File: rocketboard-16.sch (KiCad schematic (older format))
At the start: 108 parts, among them J1 SWD, K1 MX_RGB, K10 MX_RGB, K11 MX_RGB, K12 MX_RGB, K13 MX_RGB, K14 MX_RGB, K15 MX_RGB, K16 MX_RGB, K2 MX_RGB, K3 MX_RGB, K4 MX_RGB, K5 MX_RGB, K6 MX_RGB, K7 MX_RGB, K8 MX_RGB, K9 MX_RGB, P1 USB_C_Plug_USB2.0, SW1 SW_Push, SW2 Rotary 1, SW3 Rotary 2, U1 STM32F103C8T6, U2 AMS1117-3.3, U3 USBLC6-2SC6, U4 SSD1306_128x64, X1 8 MHz, Y1 32.768 kHz

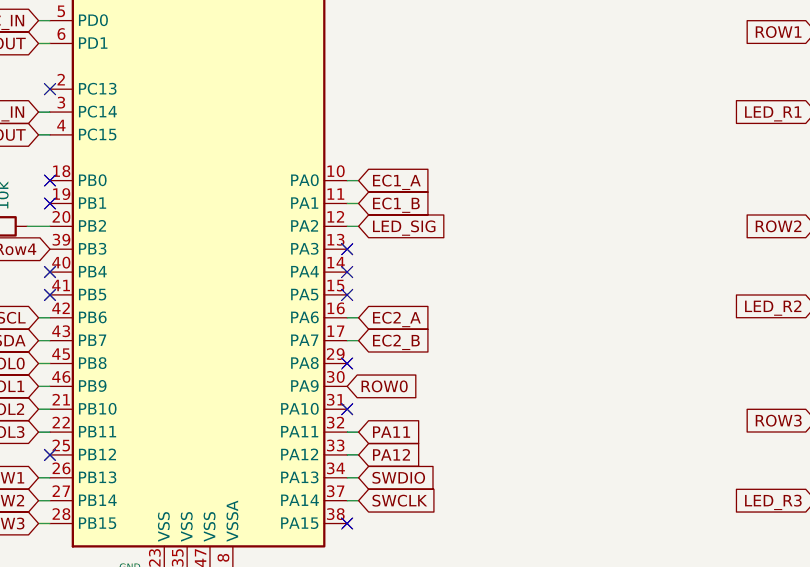
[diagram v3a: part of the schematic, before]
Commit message: Routed more traces. Only lacking a few more connections except for ground. Had to move some pins around to make room, though the change did not help with routing so far.
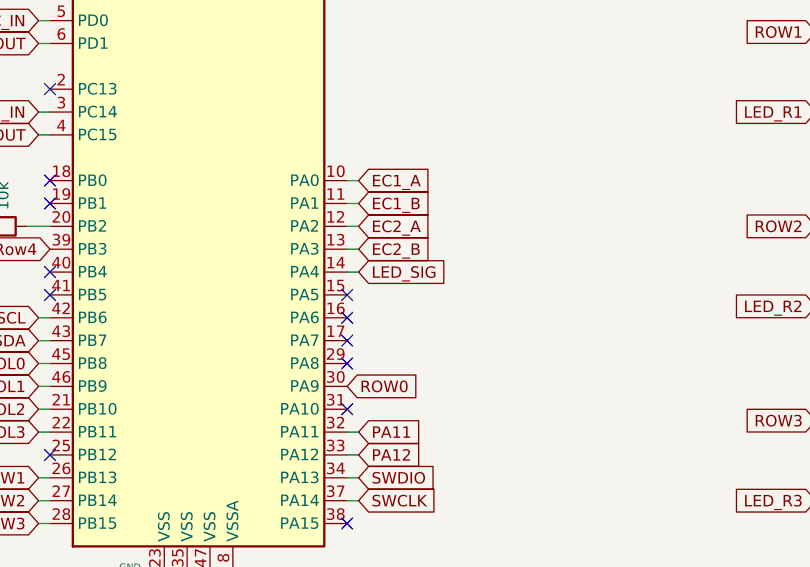
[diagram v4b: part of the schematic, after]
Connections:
- net EC2_A: now also U1.12 (PA2); no longer U1.16 (PA6)
- net EC2_B: now also U1.13 (PA3); no longer U1.17 (PA7)
- net LED_SIG: now also U1.14 (PA4); no longer U1.12 (PA2)
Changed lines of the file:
@@
 Text GLabel 9700 1150 2    50   Input ~ 0
 EC2_A
-Text GLabel 3200 3800 2    50   Input ~ 0
+Text GLabel 3200 3400 2    50   Input ~ 0
 EC2_A
-Text GLabel 3200 3900 2    50   Input ~ 0
+Text GLabel 3200 3500 2    50   Input ~ 0
 EC2_B
 $Comp
@@
 	2750 5500 2950 5500
 Connection ~ 2750 5700
-Text GLabel 3200 3400 2    50   Input ~ 0
+Text GLabel 3200 3600 2    50   Input ~ 0
 LED_SIG
 Text GLabel 5200 2050 0    50   Input ~ 0
@@
 Wire Wire Line
 	2850 1150 3100 1150
-Text GLabel 3200 3300 2    50   Input ~ 0
-EC1_B
-Text GLabel 3200 3200 2    50   Input ~ 0
-EC1_A
 Wire Wire Line
 	5400 950  5250 950
@@
 Wire Wire Line
 	9550 1050 9650 1050
-NoConn ~ 3150 3600
 Text GLabel 5200 5100 0    50   Input ~ 0
 Row4
@@
 Wire Wire Line
 	3200 3400 3150 3400
-Wire Wire Line
-	3200 3800 3150 3800
-Wire Wire Line
-	3150 3900 3200 3900
 Wire Wire Line
 	3200 4300 3150 4300
@@
 Wire Wire Line
 	6450 6300 6450 5900
-NoConn ~ 3150 3500
 NoConn ~ 1850 4400
+Text GLabel 3200 3200 2    50   Input ~ 0
+EC1_A
+Text GLabel 3200 3300 2    50   Input ~ 0
+EC1_B
+Wire Wire Line
+	3200 3500 3150 3500
+Wire Wire Line
+	3150 3600 3200 3600
+NoConn ~ 3150 3900
+NoConn ~ 3150 3800
 $EndSCHEMATC

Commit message: Updated symbols and footprints to use project specific files (portability). Changed one via, was only one smaller than rest.
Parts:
- C1, C11, C12, C14, C15, C16, C17, C18, C19, C2, C20, C21, C22, C23, C24, C25, C26, C27, C28, C29, C3, C30, C31, C4, C5, C6, C7, C8, C9: symbol rocketboard-16-rescue:C_Small-Device-num_macro_pad-rescue -> Device:C_Small
- D1, D10, D11, D12, D13, D14, D15, D16, D17, D18, D19, D2, D3, D4, D5, D6, D7, D8, D9: symbol rocketboard-16-rescue:D-Device-num_macro_pad-rescue -> Device:D
- D20, D21, D22, D23, D24, D25, D26, D27, D28, D29, D30, D31, D32, D33, D34, D35: footprint josh-keyboard:DUMMY_SK6812MINI-E -> seth-keyboard:DUMMY_SK6812MINI-E
- H1, H2, H3, H4: symbol rocketboard-16-rescue:MountingHole-Mechanical-num_macro_pad-rescue -> Mechanical:MountingHole
- J1: symbol rocketboard-16-rescue:Conn_01x04-Connector_Generic-num_macro_pad-rescue -> Connector_Generic:Conn_01x04
- K1, K10, K11, K12, K13, K14, K15, K16, K2, K3, K4, K5, K6, K7, K8, K9: footprint josh-keyboard:MX_KEYSWITCH_RGB_2D -> seth-keyboard:MX_KEYSWITCH_RGB_2D; symbol josh-keyboard:MX_RGB -> seth-keyboard:MX_RGB
- P1: footprint josh-connectors:USB_C_U262-161N-4BVC11 -> seth-connectors:USB_C_U262-161N-4BVC11
- R1, R2, R3, R4, R5, R6, R7, R8, R9: symbol rocketboard-16-rescue:R-Device-num_macro_pad-rescue -> Device:R
- SW1: symbol rocketboard-16-rescue:SW_Push-Switch-num_macro_pad-rescue -> Switch:SW_Push
- SW2, SW3: footprint josh-buttons-switches:RotaryEncoder_Alps_EC11E-Switch_Vertical_H20mm_CircularMountingHoles -> seth-buttons:RotaryEncoder_Alps_EC11E-Switch_Vertical_H20mm_CircularMountingHoles
- U1: symbol rocketboard-16-rescue:STM32F103C8Tx-MCU_ST_STM32F1-num_macro_pad-rescue -> MCU_ST_STM32F1:STM32F103C8Tx
- U2: symbol rocketboard-16-rescue:AMS1117-3.3-Regulator_Linear-num_macro_pad-rescue -> Regulator_Linear:AMS1117-3.3
- X1: symbol keyboard_parts:XTAL_GND -> Device:Crystal_GND24; Part_num (none) -> X50328MSB4SI
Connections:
- net GND: now also X1.2, X1.4; no longer X1.3
- net at C2.1, R7.1: now also X1.3; no longer X1.2

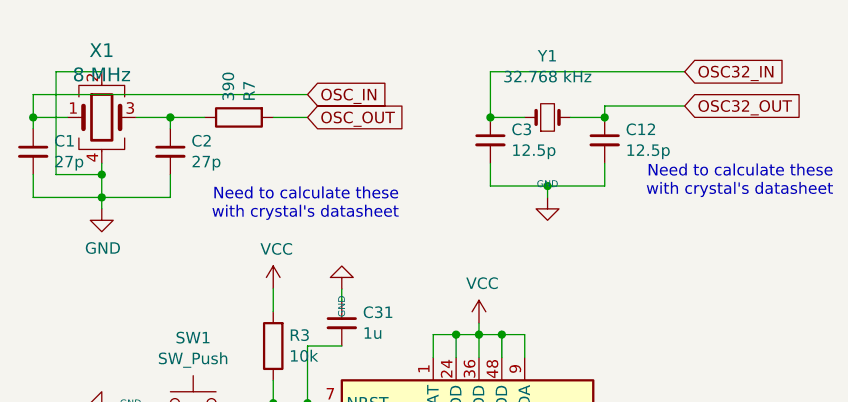
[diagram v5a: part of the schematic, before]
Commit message: Updated schematic and pcb as I found specific parts for BOM, now board needs routing for the diodes on the switches. Created a BOM spreadsheet for manual entry of part numbers, venders, prices, etc.
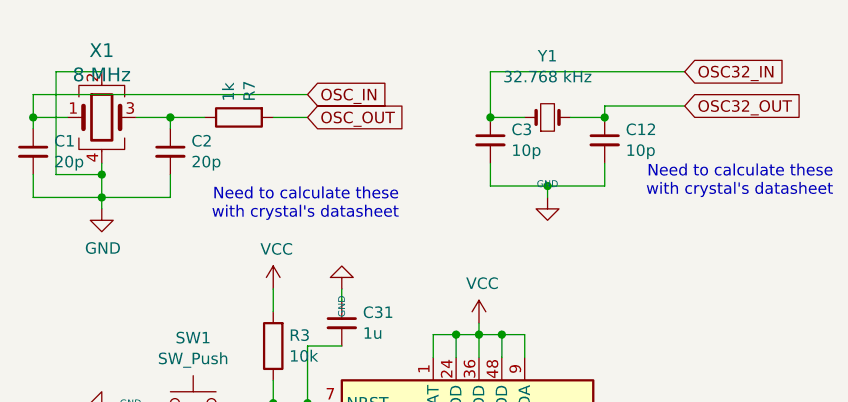
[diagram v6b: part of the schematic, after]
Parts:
- C1, C2: value 27p -> 20p
- C10: footprint Capacitor_SMD:C_0805_2012Metric -> Capacitor_Tantalum_SMD:CP_EIA-3216-10_Kemet-I
- C12, C3: value 12.5p -> 10p
- D1, D10, D11, D12, D13, D14, D15, D16, D17, D18, D19, D2, D3, D4, D5, D6, D7, D8, D9: footprint Diode_SMD:D_0603_1608Metric -> Diode_SMD:D_SOD-123
- R7: value 390 -> 1k
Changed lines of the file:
@@
 P 600 1000
 F 0 "C1" H 692 1046 50  0000 L CNN
-F 1 "27p" H 692 955 50  0000 L CNN
+F 1 "20p" H 692 955 50  0000 L CNN
 F 2 "Capacitor_SMD:C_0603_1608Metric" H 600 1000 50  0001 C CNN
 F 3 "~" H 600 1000 50  0001 C CNN
@@
 P 1200 1000
 F 0 "C2" H 1292 1046 50  0000 L CNN
-F 1 "27p" H 1292 955 50  0000 L CNN
+F 1 "20p" H 1292 955 50  0000 L CNN
 F 2 "Capacitor_SMD:C_0603_1608Metric" H 1200 1000 50  0001 C CNN
 F 3 "~" H 1200 1000 50  0001 C CNN
@@
 F 0 "D17" H 2000 5283 50  0000 C CNN
 F 1 "D" H 2000 5374 50  0000 C CNN
-F 2 "Diode_SMD:D_0603_1608Metric" H 2000 5500 50  0001 C CNN
+F 2 "Diode_SMD:D_SOD-123" H 2000 5500 50  0001 C CNN
 F 3 "~" H 2000 5500 50  0001 C CNN
 	1    2000 5500
@@
 F 0 "C10" H 2838 5646 50  0000 L CNN
 F 1 "1u" H 2838 5555 50  0000 L CNN
-F 2 "Capacitor_SMD:C_0805_2012Metric" H 2750 5600 50  0001 C CNN
+F 2 "Capacitor_Tantalum_SMD:CP_EIA-3216-10_Kemet-I" H 2750 5600 50  0001 C CNN
 F 3 "~" H 2750 5600 50  0001 C CNN
 	1    2750 5600
@@
 P 1500 850
 F 0 "R7" H 1430 804 50  0000 R CNN
-F 1 "390" H 1430 895 50  0000 R CNN
+F 1 "1k" H 1430 895 50  0000 R CNN
 F 2 "Resistor_SMD:R_0603_1608Metric" V 1430 850 50  0001 C CNN
 F 3 "~" H 1500 850 50  0001 C CNN
@@
 OSC_OUT
 $Comp
-L Device:Crystal_Small Y1
-U 1 1 5F58060E
-P 2850 850
-F 0 "Y1" H 2850 1118 50  0000 C CNN
-F 1 "32.768 kHz" H 2850 1027 50  0000 C CNN
-F 2 "Crystal:Crystal_SMD_3215-2Pin_3.2x1.5mm" H 2850 850 50  0001 C CNN
-F 3 "https://lcsc.com/product-detail/SMD-Crystal-Resonators_SJK-SHENZHEN-CRYSTAL-TECH-7LC32768F12UC_C252398.html" H 2850 850 50  0001 C CNN
-	1    2850 850
-	1    0    0    -1
-$EndComp
-$Comp
 L Device:C_Small C3
 U 1 1 5F5A7A41
 P 2600 950
 F 0 "C3" H 2692 996 50  0000 L CNN
-F 1 "12.5p" H 2692 905 50  0000 L CNN
+F 1 "10p" H 2692 905 50  0000 L CNN
 F 2 "Capacitor_SMD:C_0603_1608Metric" H 2600 950 50  0001 C CNN
 F 3 "~" H 2600 950 50  0001 C CNN
@@
 P 3100 950
 F 0 "C12" H 3192 996 50  0000 L CNN
-F 1 "12.5p" H 3192 905 50  0000 L CNN
+F 1 "10p" H 3192 905 50  0000 L CNN
 F 2 "Capacitor_SMD:C_0603_1608Metric" H 3100 950 50  0001 C CNN
 F 3 "~" H 3100 950 50  0001 C CNN
@@
 F 0 "D18" V 6046 1270 50  0000 R CNN
 F 1 "D" V 5955 1270 50  0000 R CNN
-F 2 "Diode_SMD:D_0603_1608Metric" H 6000 1350 50  0001 C CNN
+F 2 "Diode_SMD:D_SOD-123" H 6000 1350 50  0001 C CNN
 F 3 "~" H 6000 1350 50  0001 C CNN
 	1    6000 1350
@@
 F 0 "D19" V 8846 1270 50  0000 R CNN
 F 1 "D" V 8755 1270 50  0000 R CNN
-F 2 "Diode_SMD:D_0603_1608Metric" H 8800 1350 50  0001 C CNN
+F 2 "Diode_SMD:D_SOD-123" H 8800 1350 50  0001 C CNN
 F 3 "~" H 8800 1350 50  0001 C CNN
 	1    8800 1350
@@
 F 0 "D4" V 8196 2320 50  0000 R CNN
 F 1 "D" V 8105 2320 50  0000 R CNN
-F 2 "Diode_SMD:D_0603_1608Metric" H 8150 2400 50  0001 C CNN
+F 2 "Diode_SMD:D_SOD-123" H 8150 2400 50  0001 C CNN
 F 3 "~" H 8150 2400 50  0001 C CNN
 	1    8150 2400
@@
 F 0 "D3" V 7246 2320 50  0000 R CNN
 F 1 "D" V 7155 2320 50  0000 R CNN
-F 2 "Diode_SMD:D_0603_1608Metric" H 7200 2400 50  0001 C CNN
+F 2 "Diode_SMD:D_SOD-123" H 7200 2400 50  0001 C CNN
 F 3 "~" H 7200 2400 50  0001 C CNN
 	1    7200 2400
@@
 F 0 "D2" V 6296 2320 50  0000 R CNN
 F 1 "D" V 6205 2320 50  0000 R CNN
-F 2 "Diode_SMD:D_0603_1608Metric" H 6250 2400 50  0001 C CNN
+F 2 "Diode_SMD:D_SOD-123" H 6250 2400 50  0001 C CNN
 F 3 "~" H 6250 2400 50  0001 C CNN
 	1    6250 2400
@@
 F 0 "D1" V 5346 2320 50  0000 R CNN
 F 1 "D" V 5255 2320 50  0000 R CNN
-F 2 "Diode_SMD:D_0603_1608Metric" H 5300 2400 50  0001 C CNN
+F 2 "Diode_SMD:D_SOD-123" H 5300 2400 50  0001 C CNN
 F 3 "~" H 5300 2400 50  0001 C CNN
 	1    5300 2400
@@
 F 0 "D8" V 8196 3170 50  0000 R CNN
 F 1 "D" V 8105 3170 50  0000 R CNN
-F 2 "Diode_SMD:D_0603_1608Metric" H 8150 3250 50  0001 C CNN
+F 2 "Diode_SMD:D_SOD-123" H 8150 3250 50  0001 C CNN
 F 3 "~" H 8150 3250 50  0001 C CNN
 	1    8150 3250
@@
 F 0 "D7" V 7246 3170 50  0000 R CNN
 F 1 "D" V 7155 3170 50  0000 R CNN
-F 2 "Diode_SMD:D_0603_1608Metric" H 7200 3250 50  0001 C CNN
+F 2 "Diode_SMD:D_SOD-123" H 7200 3250 50  0001 C CNN
 F 3 "~" H 7200 3250 50  0001 C CNN
 	1    7200 3250
@@
 F 0 "D6" V 6296 3170 50  0000 R CNN
 F 1 "D" V 6205 3170 50  0000 R CNN
-F 2 "Diode_SMD:D_0603_1608Metric" H 6250 3250 50  0001 C CNN
+F 2 "Diode_SMD:D_SOD-123" H 6250 3250 50  0001 C CNN
 F 3 "~" H 6250 3250 50  0001 C CNN
 	1    6250 3250
@@
 F 0 "D5" V 5346 3170 50  0000 R CNN
 F 1 "D" V 5255 3170 50  0000 R CNN
-F 2 "Diode_SMD:D_0603_1608Metric" H 5300 3250 50  0001 C CNN
+F 2 "Diode_SMD:D_SOD-123" H 5300 3250 50  0001 C CNN
 F 3 "~" H 5300 3250 50  0001 C CNN
 	1    5300 3250
@@
 F 0 "D12" V 8196 4020 50  0000 R CNN
 F 1 "D" V 8105 4020 50  0000 R CNN
-F 2 "Diode_SMD:D_0603_1608Metric" H 8150 4100 50  0001 C CNN
+F 2 "Diode_SMD:D_SOD-123" H 8150 4100 50  0001 C CNN
 F 3 "~" H 8150 4100 50  0001 C CNN
 	1    8150 4100
@@
 F 0 "D11" V 7246 4020 50  0000 R CNN
 F 1 "D" V 7155 4020 50  0000 R CNN
-F 2 "Diode_SMD:D_0603_1608Metric" H 7200 4100 50  0001 C CNN
+F 2 "Diode_SMD:D_SOD-123" H 7200 4100 50  0001 C CNN
 F 3 "~" H 7200 4100 50  0001 C CNN
 	1    7200 4100
@@
 F 0 "D10" V 6296 4020 50  0000 R CNN
 F 1 "D" V 6205 4020 50  0000 R CNN
-F 2 "Diode_SMD:D_0603_1608Metric" H 6250 4100 50  0001 C CNN
+F 2 "Diode_SMD:D_SOD-123" H 6250 4100 50  0001 C CNN
 F 3 "~" H 6250 4100 50  0001 C CNN
 	1    6250 4100
@@
 F 0 "D9" V 5346 4020 50  0000 R CNN
 F 1 "D" V 5255 4020 50  0000 R CNN
-F 2 "Diode_SMD:D_0603_1608Metric" H 5300 4100 50  0001 C CNN
+F 2 "Diode_SMD:D_SOD-123" H 5300 4100 50  0001 C CNN
 F 3 "~" H 5300 4100 50  0001 C CNN
 	1    5300 4100
@@
 F 0 "D16" V 8196 4870 50  0000 R CNN
 F 1 "D" V 8105 4870 50  0000 R CNN
-F 2 "Diode_SMD:D_0603_1608Metric" H 8150 4950 50  0001 C CNN
+F 2 "Diode_SMD:D_SOD-123" H 8150 4950 50  0001 C CNN
 F 3 "~" H 8150 4950 50  0001 C CNN
 	1    8150 4950
@@
 F 0 "D15" V 7246 4870 50  0000 R CNN
 F 1 "D" V 7155 4870 50  0000 R CNN
-F 2 "Diode_SMD:D_0603_1608Metric" H 7200 4950 50  0001 C CNN
+F 2 "Diode_SMD:D_SOD-123" H 7200 4950 50  0001 C CNN
 F 3 "~" H 7200 4950 50  0001 C CNN
 	1    7200 4950
@@
 F 0 "D14" V 6296 4870 50  0000 R CNN
 F 1 "D" V 6205 4870 50  0000 R CNN
-F 2 "Diode_SMD:D_0603_1608Metric" H 6250 4950 50  0001 C CNN
+F 2 "Diode_SMD:D_SOD-123" H 6250 4950 50  0001 C CNN
 F 3 "~" H 6250 4950 50  0001 C CNN
 	1    6250 4950
@@
 F 0 "D13" V 5346 4870 50  0000 R CNN
 F 1 "D" V 5255 4870 50  0000 R CNN
-F 2 "Diode_SMD:D_0603_1608Metric" H 5300 4950 50  0001 C CNN
+F 2 "Diode_SMD:D_SOD-123" H 5300 4950 50  0001 C CNN
 F 3 "~" H 5300 4950 50  0001 C CNN
 	1    5300 4950
@@
 	900  1100 900  1200
 Connection ~ 900  1100
+$Comp
+L Device:Crystal_Small Y1
+U 1 1 5F58060E
+P 2850 850
+F 0 "Y1" H 2850 1118 50  0000 C CNN
+F 1 "32.768 kHz" H 2850 1027 50  0000 C CNN
+F 2 "Crystal:Crystal_SMD_3215-2Pin_3.2x1.5mm" H 2850 850 50  0001 C CNN
+F 3 "https://datasheet.lcsc.com/szlcsc/Seiko-Epson-Q13FC1350000200_C48615.pdf" H 2850 850 50  0001 C CNN
+	1    2850 850
+	1    0    0    -1
+$EndComp
 $EndSCHEMATC

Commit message: Finished adding items to the BOM, added a tactile switch from JLCPCB footprint instead of the one I had
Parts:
- SW1: footprint Button_Switch_SMD:SW_Push_1P1T_NO_6x6mm_H9.5mm -> seth-tactile-switch:SW_TS-1187A-B-A-B
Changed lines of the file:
@@
 F 0 "SW1" H 1300 2385 50  0000 C CNN
 F 1 "SW_Push" H 1300 2294 50  0000 C CNN
-F 2 "Button_Switch_SMD:SW_Push_1P1T_NO_6x6mm_H9.5mm" H 1300 2300 50  0001 C CNN
+F 2 "seth-tactile-switch:SW_TS-1187A-B-A-B" H 1300 2300 50  0001 C CNN
 F 3 "~" H 1300 2300 50  0001 C CNN
 	1    1300 2100

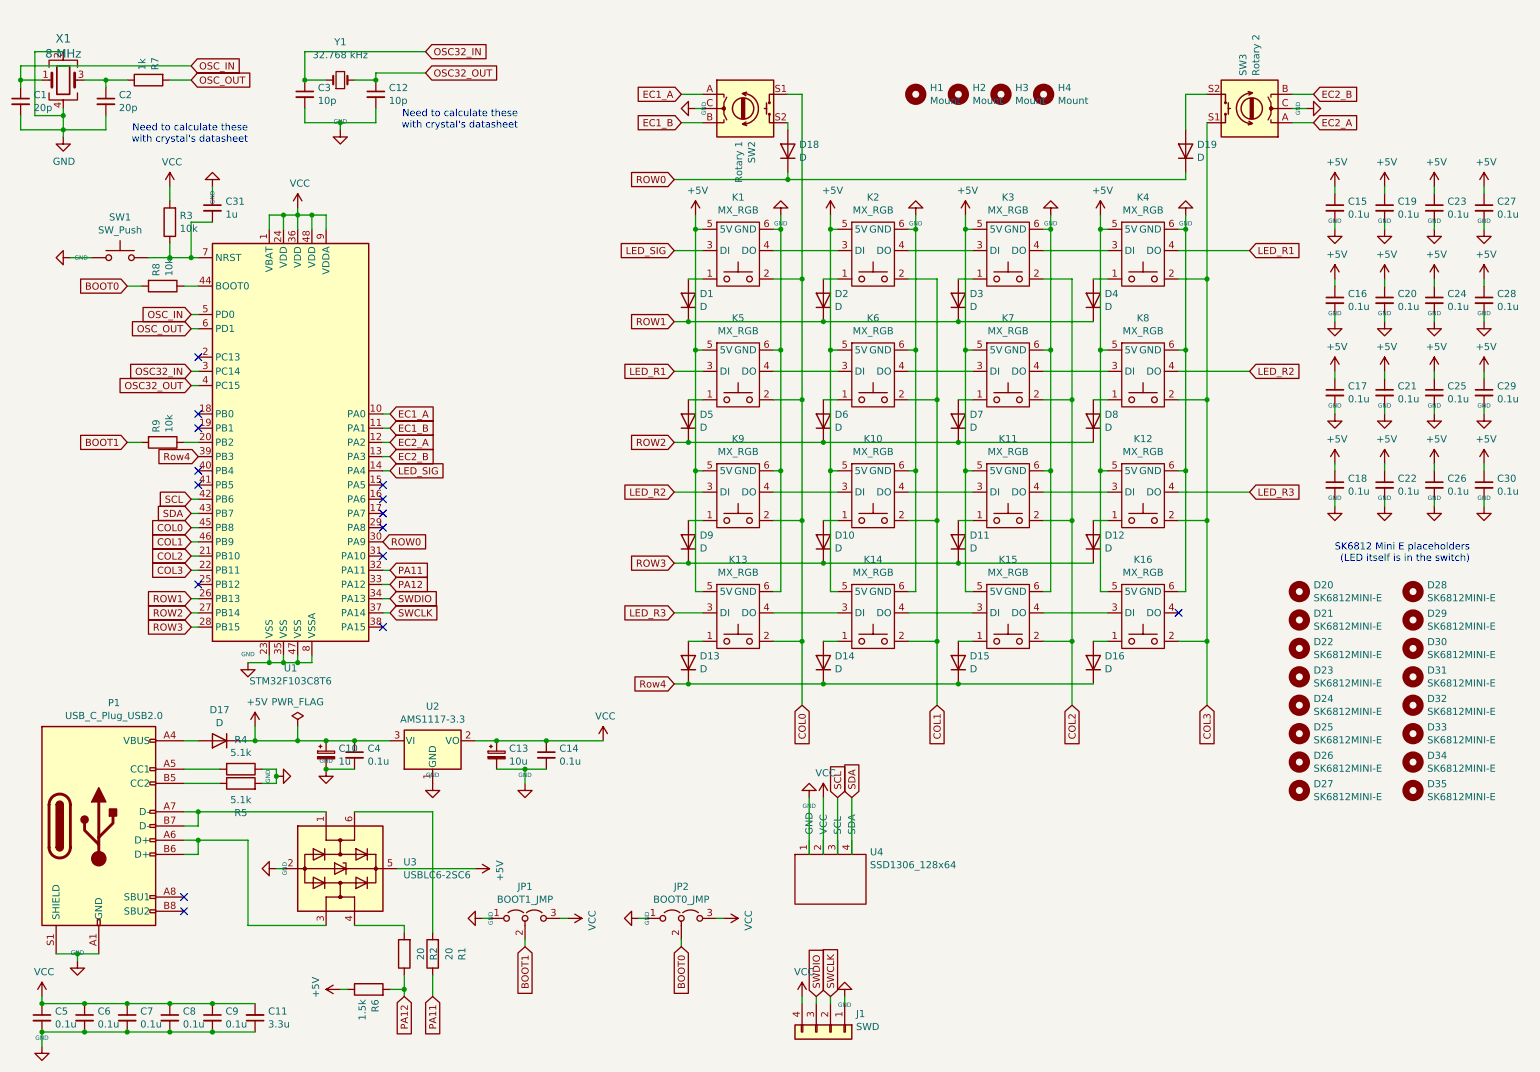
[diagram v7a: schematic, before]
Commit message: Updated the graphics, added some more, and made some slight changed to some components
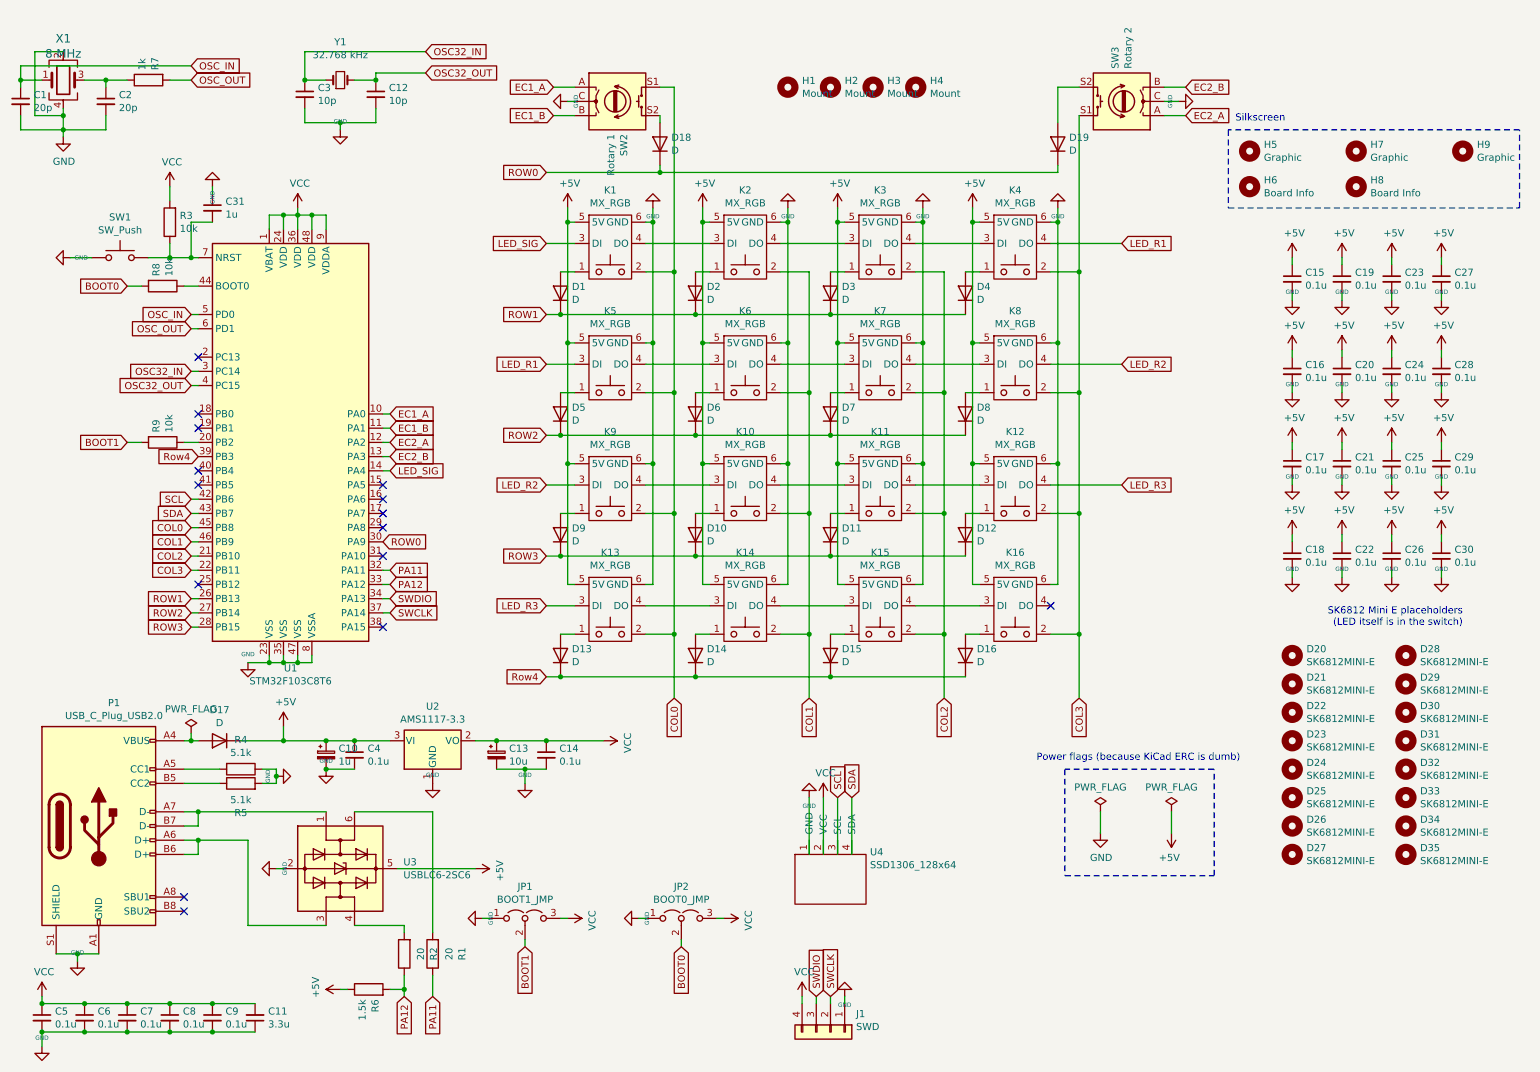
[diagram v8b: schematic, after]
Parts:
- added H5: Graphic, seth-logo:saturn_v_simplified, symbol Mechanical:MountingHole
- added H6: Board Info, seth-logo:board-title, symbol Mechanical:MountingHole
- added H7: Graphic, seth-logo:lunar_module, symbol Mechanical:MountingHole
- added H8: Board Info, seth-logo:text, symbol Mechanical:MountingHole
- added H9: Graphic, seth-logo:space_shuttle, symbol Mechanical:MountingHole
- C13: footprint Capacitor_SMD:C_0805_2012Metric -> Capacitor_Tantalum_SMD:CP_EIA-3216-10_Kemet-I
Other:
- note added: "Power flags (because KiCad ERC is dumb)"
- note added: "Silkscreen"
- note removed: "Need to calculate these \nwith crystal's datasheet\n"
- moved on the sheet: C15, C16, C17, C18, C19, C20, C21, C22, C23, C24, C25, C26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
